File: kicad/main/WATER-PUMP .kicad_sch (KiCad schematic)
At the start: 12 parts, among them Q10 AO3401, Q8 AO3401

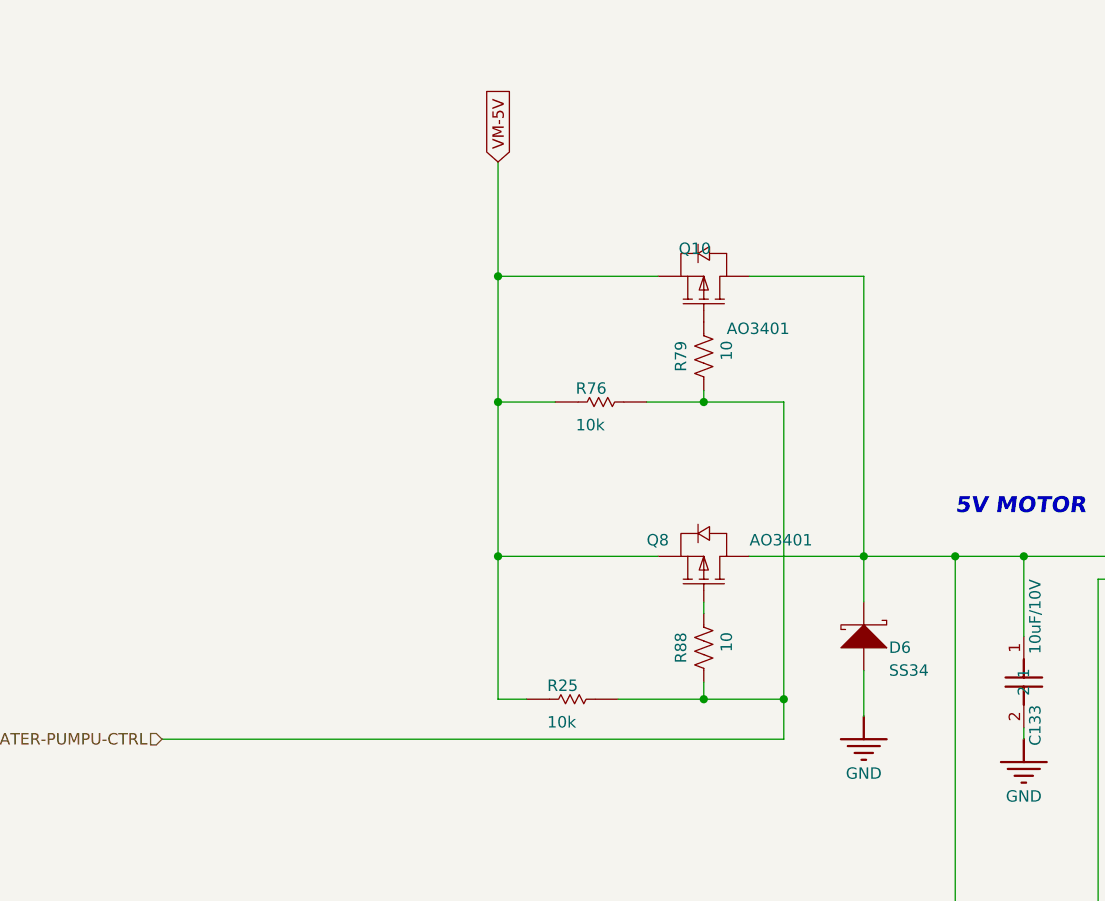
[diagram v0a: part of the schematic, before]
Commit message: Update Power Control sch, Charger sch, Speaker + Mic, JTAG and Watch Dog
**Power Control:** Replaced the BJT with a MOSFET. The MCU hang condition is not covered yet.
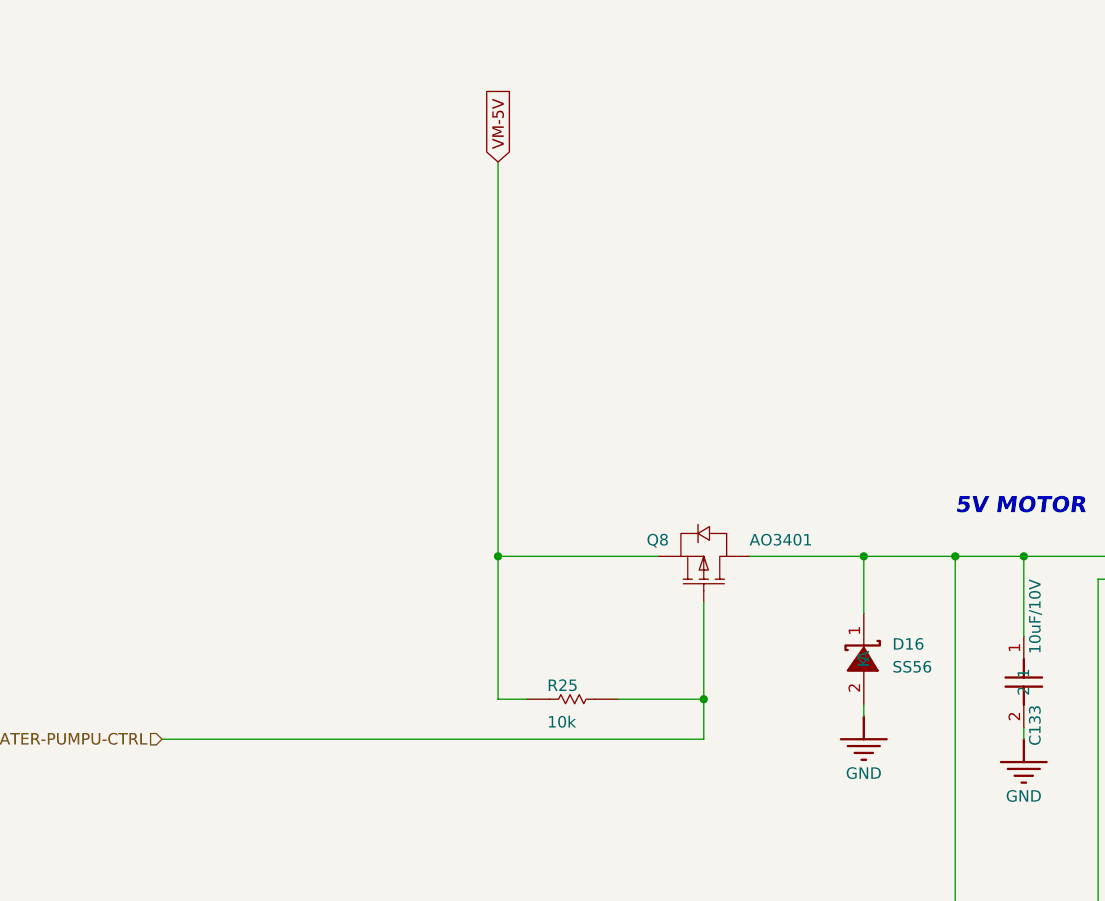
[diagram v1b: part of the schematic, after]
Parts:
- removed D6: SS34, Diode_SMD:D_SMA, symbol DesignLibrary:WATER-PUMP_1_DIODE-2_DesignLibrary.SchLib
- removed Q10: AO3401, oomwoo_altium:SOT23-3D, symbol DesignLibrary:WATER-PUMP_1_mirrored_P-MOS-SOT23_DesignLibrary.SchLib
- removed R76: 10k, Resistor_SMD:R_0603_1608Metric, symbol DesignLibrary:WATER-PUMP_2_Resistor-1_DesignLibrary.SchLib
- removed R79, R88: 10, Resistor_SMD:R_0603_1608Metric, symbol Device:R_US
- added D16: SS56, JLCImport:SS56, symbol JLCImport:SS56
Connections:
- net GND: now also D16.2 (A)
- net WATER-PUMPU-CTRL: now also Q8.1 (G)
- net at C105.2, C133.1, PUMP1.1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: now also D16.1 (K)
